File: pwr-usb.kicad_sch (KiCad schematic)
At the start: 13 parts, among them J4 Conn_01x16, J5 Conn_01x16, P1 USB_C_Plug_USB2.0, Q1 Q_PMOS_DGS, U4 NCP1117-3.3_SOT223

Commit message: refactoring, fix typos
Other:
- title: GPS Radio Beacon: Power and USB -> GPS Radio Beacon: Power and GPS
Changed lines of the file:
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@@
   (paper "A4")
   (title_block
-    (title "GPS Radio Beacon: Power and USB")
+    (title "GPS Radio Beacon: Power and GPS")
     (date "2022-10-23")
     (rev "0.1.2")

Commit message: redesign pim
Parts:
- C4: renamed from C19; footprint (none) -> Capacitor_THT:CP_Radial_Tantal_D5.0mm_P2.50mm
- C5: renamed from C20; footprint (none) -> Capacitor_THT:CP_Radial_Tantal_D5.0mm_P2.50mm
- D1: renamed from D2; footprint (none) -> LED_THT:LED_D5.0mm-4_RGB
- D2: renamed from D3; footprint (none) -> Diode_SMD:D_SOD-323_HandSoldering
- D3: renamed from D4; footprint (none) -> Diode_SMD:D_SOD-323_HandSoldering
- J1: renamed from J4; footprint (none) -> Connector_PinHeader_2.54mm:PinHeader_1x16_P2.54mm_Vertical
- J2: renamed from J5; footprint (none) -> Connector_PinHeader_2.54mm:PinHeader_1x16_P2.54mm_Vertical
- P1: footprint (none) -> Connector_USB:USB_C_Receptacle_GCT_USB4085
- Q1: footprint (none) -> Package_TO_SOT_SMD:SC-59_Handsoldering
- R3: renamed from R8; footprint (none) -> Resistor_SMD:R_0805_2012Metric_Pad1.20x1.40mm_HandSolder
- R4: renamed from R9; footprint (none) -> Resistor_SMD:R_0805_2012Metric_Pad1.20x1.40mm_HandSolder
- TP2: footprint (none) -> TestPoint:TestPoint_Loop_D2.54mm_Drill1.5mm_Beaded
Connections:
- net GND: no longer P1.S1 (SHIELD)

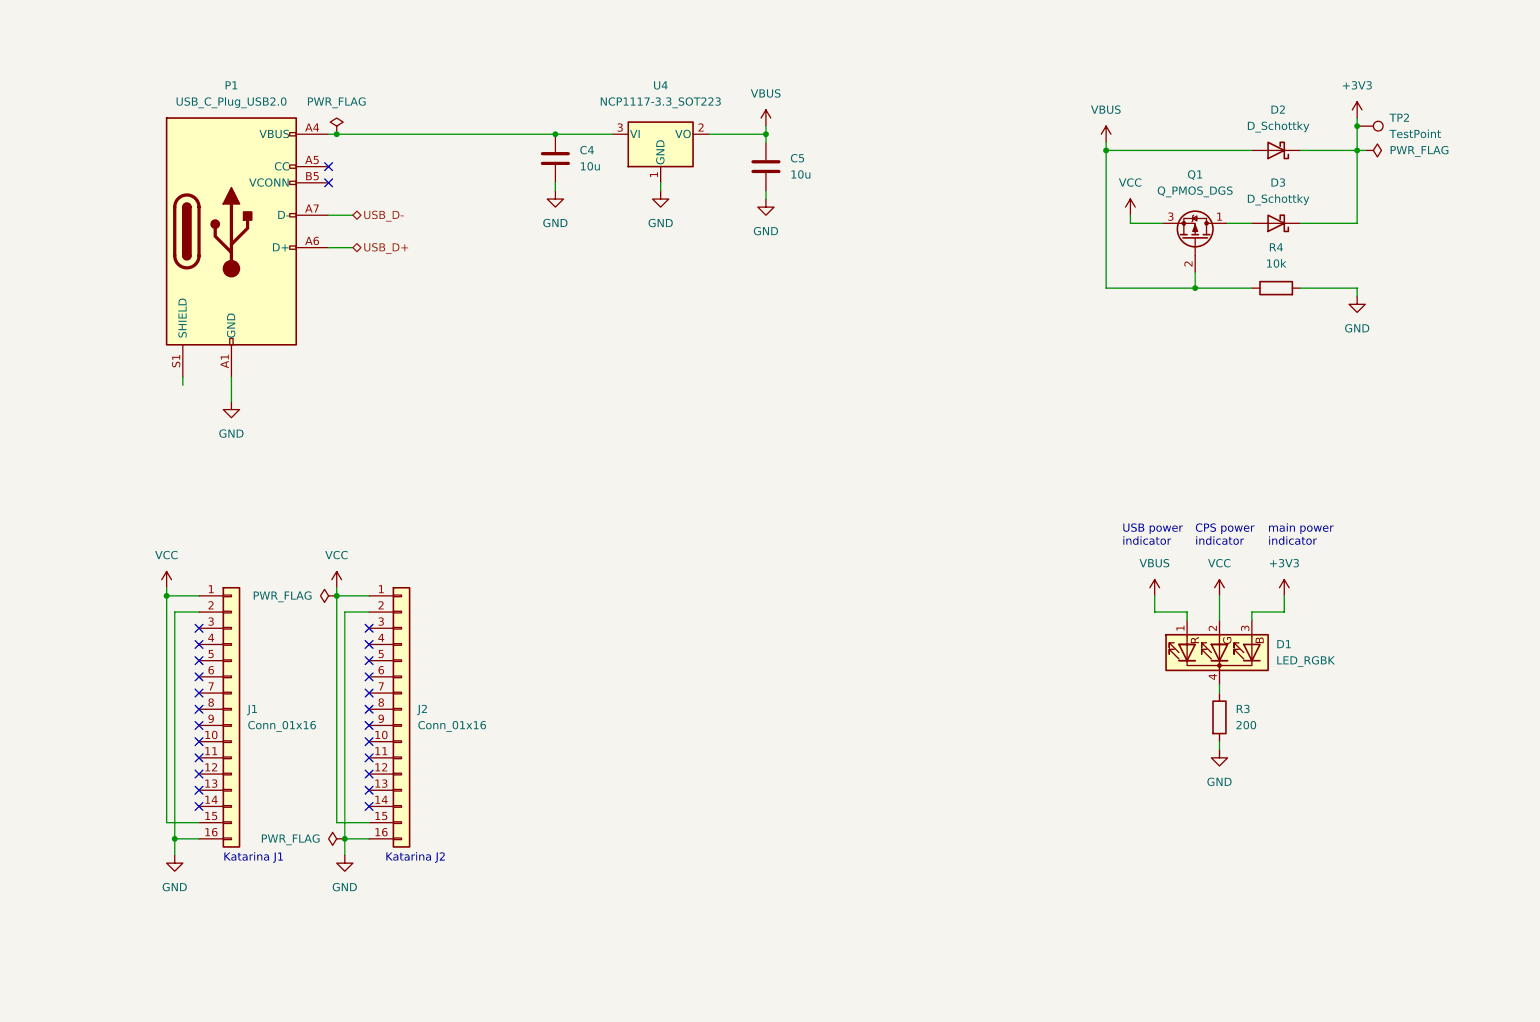
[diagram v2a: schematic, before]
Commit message: redesign for use with RFM95
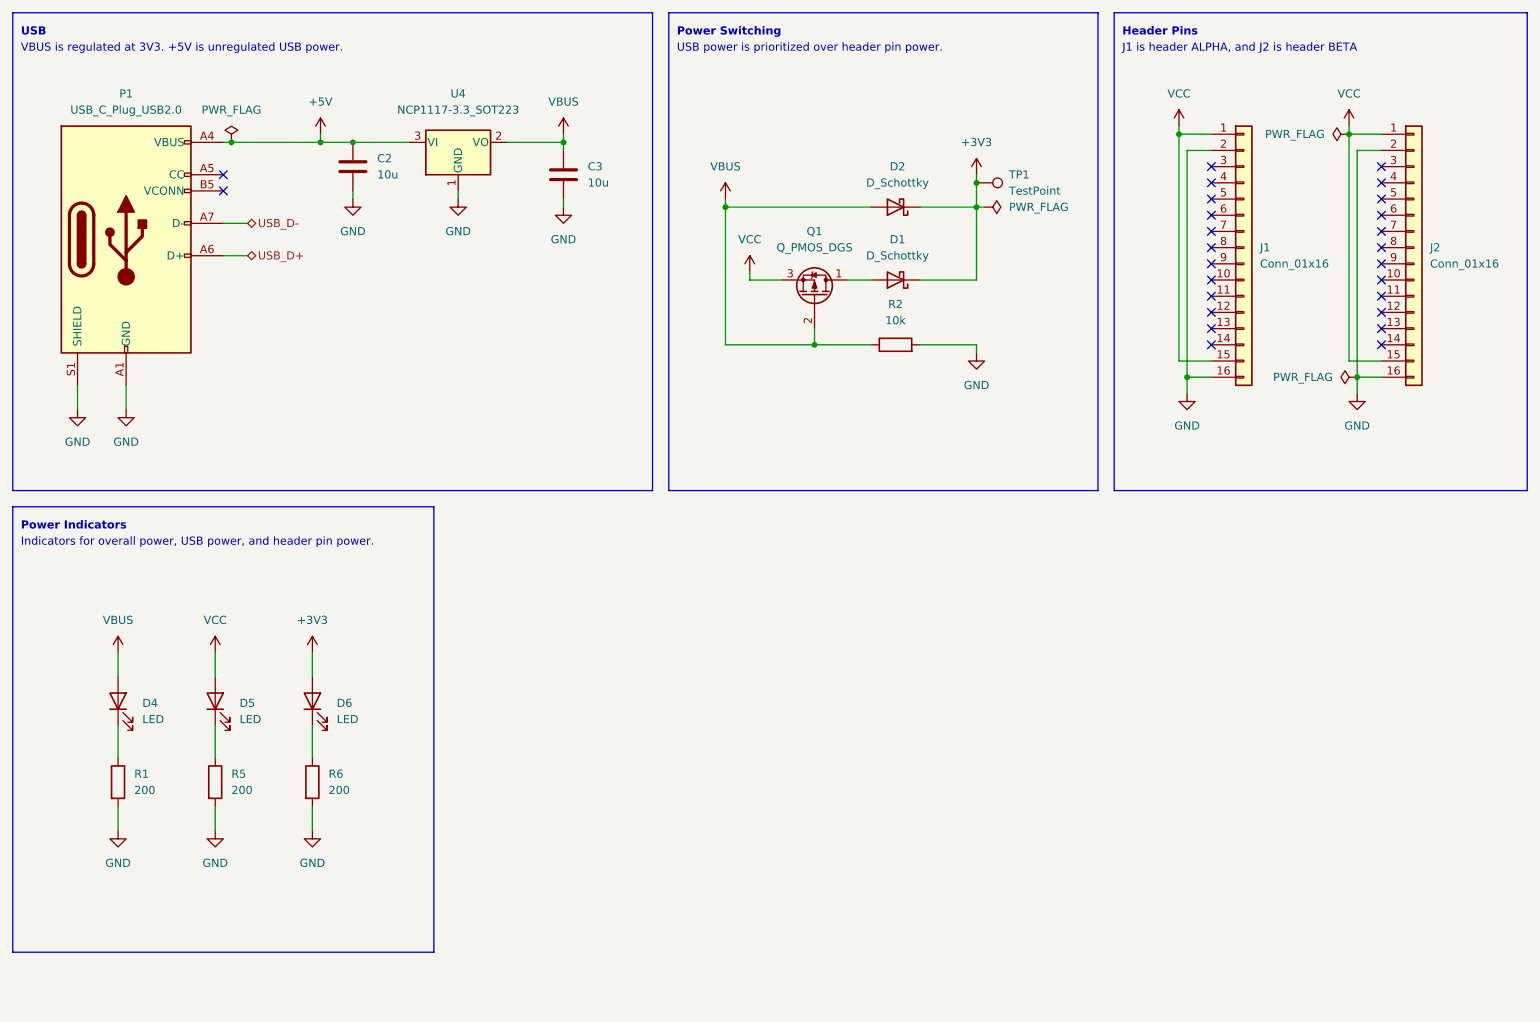
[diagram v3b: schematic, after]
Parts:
- removed D1: LED_RGBK, LED_THT:LED_D5.0mm-4_RGB, symbol Device:LED_RGBK
- added D4, D5, D6: LED, LED_THT:LED_D3.0mm, symbol Device:LED
- added R5, R6: 200, Resistor_SMD:R_0805_2012Metric_Pad1.20x1.40mm_HandSolder, symbol Device:R
- C2: renamed from C4; footprint Capacitor_THT:CP_Radial_Tantal_D5.0mm_P2.50mm -> Capacitor_SMD:C_1206_3216Metric_Pad1.33x1.80mm_HandSolder
- C3: renamed from C5; footprint Capacitor_THT:CP_Radial_Tantal_D5.0mm_P2.50mm -> Capacitor_SMD:C_1206_3216Metric_Pad1.33x1.80mm_HandSolder
- renumbered D3 to D1, R3 to R1, R4 to R2, TP2 to TP1
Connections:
- net +3V3: now also D6.2 (A)
- net GND: now also P1.S1 (SHIELD), R5.2, R6.2
- net VBUS: now also D4.2 (A)
- net VCC: now also D5.2 (A)
- net at R1.1: now also D4.1 (K)
- net +5V: now reaches C2.1, P1.A4 (VBUS), P1.A9 (VBUS), P1.B4 (VBUS), P1.B9 (VBUS), U4.3 (VI)
- new net: D6.1 (K), R6.1
- new net: D5.1 (K), R5.1
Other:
- note added: "Header Pins"
- note added: "Indicators for overall power, USB power, and header pin power."
- note added: "J1 is header ALPHA, and J2 is header BETA"
- note added: "Power Indicators"
- note added: "Power Switching"
- note added: "USB"
- note added: "USB power is prioritized over header pin power."
- note added: "VBUS is regulated at 3V3. +5V is unregulated USB power."
- note removed: "CPS power indicator"
- note removed: "Katarina J1"
- note removed: "Katarina J2"
- note removed: "USB power indicator"
- note removed: "main power indicator"
- title: GPS Radio Beacon: Power and GPS -> GPS Radio Beacon
- moved on the sheet: C2, C3, D1, D2, J1, J2, P1, Q1, R1, R2, TP1, U4

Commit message: final updates!
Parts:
- added JP1: SolderJumper_2_Bridged, symbol Jumper:SolderJumper_2_Bridged
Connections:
- net GND: now also JP1.1 (A); no longer P1.S1 (SHIELD)
- net USB_D+: now also P1.B6
- net USB_D-: now also P1.B7
- new net: JP1.2 (B), P1.S1 (SHIELD)
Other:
- moved on the sheet: D4, D5, D6, R1, R5, R6

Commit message: Add BOOTSEL button
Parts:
- JP1: footprint (none) -> Jumper:SolderJumper-2_P1.3mm_Bridged_RoundedPad1.0x1.5mm
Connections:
- net USB_D+: no longer P1.B6
- net USB_D-: no longer P1.B7
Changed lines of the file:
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@@
   (title_block
     (title "GPS Radio Beacon")
-    (date "2022-11-28")
-    (rev "0.2.0")
+    (date "2023-01-12")
+    (rev "0.2.1")
     (company "Cornell Rocketry Team")
     (comment 1 "William Barkoff [wb273]")
+    (comment 4 "Licensed under CERN-OHL-W v2")
   )
   (junction (at 201.93 36.83) (diameter 0) (color 0 0 0 0)
@@
       (effects (font (size 1.27 1.27)) (justify right))
     )
-    (property "Footprint" "" (id 2) (at 29.21 91.44 0)
+    (property "Footprint" "Jumper:SolderJumper-2_P1.3mm_Bridged_RoundedPad1.0x1.5mm" (id 2) (at 29.21 91.44 0)
       (effects (font (size 1.27 1.27)) hide)
     )
@@
     (pin "B4")
     (pin "B5")
-    (pin "B6")
-    (pin "B7")
     (pin "B9")
     (pin "S1")

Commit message: Fix many bugs with the initial version
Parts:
- removed C2, C3: 10u, Capacitor_SMD:C_1206_3216Metric_Pad1.33x1.80mm_HandSolder, symbol Device:C
- removed D1, D2: D_Schottky, Diode_SMD:D_SOD-323_HandSoldering, symbol Device:D_Schottky
- removed Q1: Q_PMOS_DGS, Package_TO_SOT_SMD:SC-59_Handsoldering, symbol Device:Q_PMOS_DGS
- removed R2: 10k, Resistor_SMD:R_0805_2012Metric_Pad1.20x1.40mm_HandSolder, symbol Device:R
- removed TP1: TestPoint, TestPoint:TestPoint_Loop_D2.54mm_Drill1.5mm_Beaded, symbol Connector:TestPoint
- removed U4: NCP1117-3.3_SOT223, Package_TO_SOT_SMD:SOT-223-3_TabPin2, symbol Regulator_Linear:NCP1117-3.3_SOT223
- added U4: AZ1117-3.3, Package_TO_SOT_SMD:SOT-223-3_TabPin2, symbol Regulator_Linear:AZ1117-3.3
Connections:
- net +5V is gone; now on net VBUS: P1.A4 (VBUS), P1.A9 (VBUS), P1.B4 (VBUS), P1.B9 (VBUS)
- net +3V3: now also U4.2 (VO)
- net GND: now also U4.1 (GND)
- net VBUS: now also U4.3 (VI)
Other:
- note removed: "Power Switching"
- note removed: "USB power is prioritized over header pin power."
- note removed: "VBUS is regulated at 3V3. +5V is unregulated USB power."
- moved on the sheet: D4, D5, D6, J1, J2, R1, R5, R6
